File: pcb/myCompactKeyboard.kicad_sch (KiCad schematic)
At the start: 292 parts, among them J1 OLED_128x64, SW1 RotaryEncoder_Switch, SW2 RotaryEncoder_Switch, U1 Raspberry_Pi_Pico

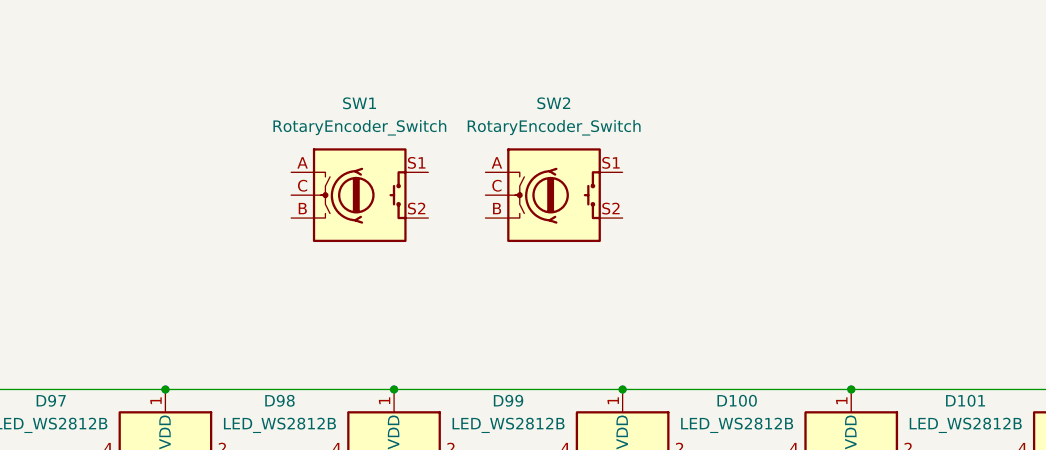
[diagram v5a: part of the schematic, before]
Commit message: added labels to rotary encoders
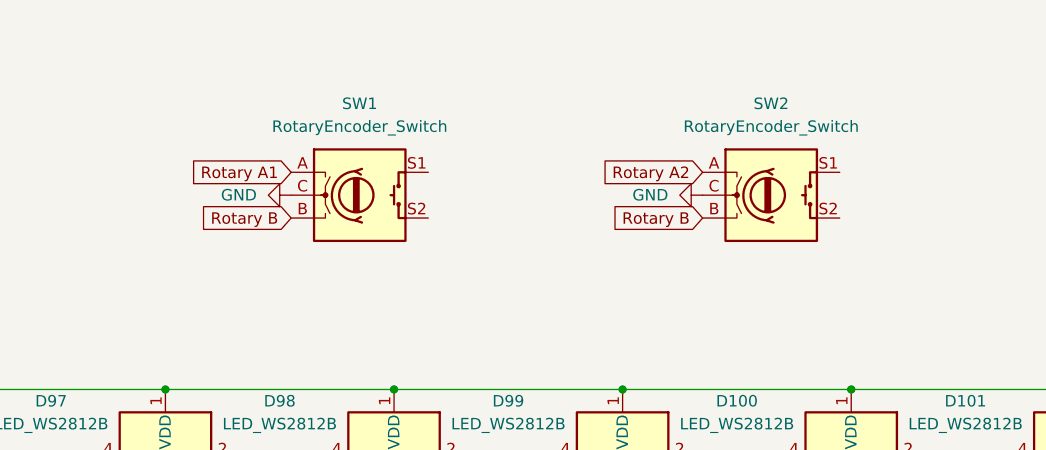
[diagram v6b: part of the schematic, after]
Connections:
- net GND: now also SW1.C, SW2.C
- net Rotary A2: now reaches SW2.A
- net Rotary B: now reaches SW2.B
- net Rotary B: now also SW1.B
- net Rotary A1: now reaches SW1.A
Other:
- moved on the sheet: SW2
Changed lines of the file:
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@@
 		)
 	)
+	(global_label "Rotary B"
+		(shape input)
+		(at 326.39 49.53 180)
+		(fields_autoplaced yes)
+		(effects
+			(font
+				(size 1.27 1.27)
+			)
+			(justify right)
+		)
+		(property "Intersheetrefs" "${INTERSHEET_REFS}"
+			(at 315.1197 49.53 0)
+			(effects
+				(font
+					(size 1.27 1.27)
+				)
+				(justify right)
+				(hide yes)
+			)
+		)
+	)
 	(global_label "Col 4"
 		(shape input)
@@
 		)
 	)
+	(global_label "Rotary A1"
+		(shape input)
+		(at 280.67 44.45 180)
+		(fields_autoplaced yes)
+		(effects
+			(font
+				(size 1.27 1.27)
+			)
+			(justify right)
+		)
+		(property "Intersheetrefs" "${INTERSHEET_REFS}"
+			(at 268.3716 44.45 0)
+			(effects
+				(font
+					(size 1.27 1.27)
+				)
+				(justify right)
+				(hide yes)
+			)
+		)
+	)
 	(global_label "Col 12"
 		(shape input)
@@
 		)
 	)
+	(global_label "Rotary B"
+		(shape input)
+		(at 280.67 49.53 180)
+		(fields_autoplaced yes)
+		(effects
+			(font
+				(size 1.27 1.27)
+			)
+			(justify right)
+		)
+		(property "Intersheetrefs" "${INTERSHEET_REFS}"
+			(at 269.3997 49.53 0)
+			(effects
+				(font
+					(size 1.27 1.27)
+				)
+				(justify right)
+				(hide yes)
+			)
+		)
+	)
 	(global_label "Col 11"
 		(shape input)
@@
 		)
 	)
+	(global_label "Rotary A2"
+		(shape input)
+		(at 326.39 44.45 180)
+		(fields_autoplaced yes)
+		(effects
+			(font
+				(size 1.27 1.27)
+			)
+			(justify right)
+		)
+		(property "Intersheetrefs" "${INTERSHEET_REFS}"
+			(at 314.0916 44.45 0)
+			(effects
+				(font
+					(size 1.27 1.27)
+				)
+				(justify right)
+				(hide yes)
+			)
+		)
+	)
 	(global_label "Row 8"
 		(shape input)
@@
 	(symbol
 		(lib_id "Device:RotaryEncoder_Switch")
-		(at 309.88 46.99 0)
+		(at 334.01 46.99 0)
 		(unit 1)
 		(exclude_from_sim no)
@@
 		(fields_autoplaced yes)
 		(property "Reference" "SW2"
-			(at 309.88 36.83 0)
+			(at 334.01 36.83 0)
 			(effects
 				(font
@@
 		)
 		(property "Value" "RotaryEncoder_Switch"
-			(at 309.88 39.37 0)
+			(at 334.01 39.37 0)
 			(effects
 				(font
@@
 		)
 		(property "Footprint" ""
-			(at 306.07 42.926 0)
+			(at 330.2 42.926 0)
 			(effects
 				(font
@@
 		)
 		(property "Datasheet" "~"
-			(at 309.88 40.386 0)
+			(at 334.01 40.386 0)
 			(effects
 				(font
@@
 		)
 		(property "Description" "Rotary encoder, dual channel, incremental quadrate outputs, with switch"
-			(at 309.88 46.99 0)
+			(at 334.01 46.99 0)
 			(effects
 				(font
@@
 	)
 	(symbol
+		(lib_id "power:GND")
+		(at 280.67 46.99 270)
+		(unit 1)
+		(exclude_from_sim no)
+		(in_bom yes)
+		(on_board yes)
+		(dnp no)
+		(fields_autoplaced yes)
+		(property "Reference" "#PWR06"
+			(at 274.32 46.99 0)
+			(effects
+				(font
+					(size 1.27 1.27)
+				)
+				(hide yes)
+			)
+		)
+		(property "Value" "GND"
+			(at 276.86 46.9899 90)
+			(effects
+				(font
+					(size 1.27 1.27)
+				)
+				(justify right)
+			)
+		)
+		(property "Footprint" ""
+			(at 280.67 46.99 0)
+			(effects
+				(font
+					(size 1.27 1.27)
+				)
+				(hide yes)
+			)
+		)
+		(property "Datasheet" ""
+			(at 280.67 46.99 0)
+			(effects
+				(font
+					(size 1.27 1.27)
+				)
+				(hide yes)
+			)
+		)
+		(property "Description" "Power symbol creates a global label with name \"GND\" , ground"
+			(at 280.67 46.99 0)
+			(effects
+				(font
+					(size 1.27 1.27)
+				)
+				(hide yes)
+			)
+		)
+		(pin "1"
+		)
+		(instances
+			(project ""
+				(path "/a5f71a14-17d5-4701-ba70-d64b25a756b2"
+					(reference "#PWR06")
+					(unit 1)
+				)
+			)
+		)
+	)
+	(symbol
 		(lib_id "ScottoKeebs:Placeholder_Diode")
 		(at 68.58 59.69 90)
@@
 					(unit 1)
 				)
+			)
+		)
+	)
+	(symbol
+		(lib_id "power:GND")
+		(at 326.39 46.99 270)
+		(unit 1)
+		(exclude_from_sim no)
+		(in_bom yes)
+		(on_board yes)
+		(dnp no)
+		(fields_autoplaced yes)
+		(property "Reference" "#PWR07"
+			(at 320.04 46.99 0)
+			(effects
+				(font
+					(size 1.27 1.27)
+				)
+				(hide yes)
+			)
+		)
+		(property "Value" "GND"
+			(at 322.58 46.9899 90)
+			(effects
+				(font
+					(size 1.27 1.27)
+				)
+				(justify right)
+			)
+		)
+		(property "Footprint" ""
+			(at 326.39 46.99 0)
+			(effects
+				(font
+					(size 1.27 1.27)
+				)
+				(hide yes)
+			)
+		)
+		(property "Datasheet" ""
+			(at 326.39 46.99 0)
+			(effects
+				(font
+					(size 1.27 1.27)
+				)
+				(hide yes)
+			)
+		)
+		(property "Description" "Power symbol creates a global label with name \"GND\" , ground"
+			(at 326.39 46.99 0)
+			(effects
+				(font
+					(size 1.27 1.27)
+				)
+				(hide yes)
+			)
+		)
+		(pin "1"
+		)
+		(instances
+			(project ""
+				(path "/a5f71a14-17d5-4701-ba70-d64b25a756b2"
+					(reference "#PWR07")
+					(unit 1)
+				)

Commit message: created pcb and placed switches
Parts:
- removed S82, S86: Keyswitch, ScottoKeebs_MX:MX_PCB_1.00u, symbol ScottoKeebs:Placeholder_Keyswitch
- SW1, SW2: footprint (none) -> Rotary_Encoder:RotaryEncoder_Alps_EC11E-Switch_Vertical_H20mm
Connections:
- net +5V: now also J1.2 (VCC)
- net Col 10: now also SW2.S1
- net Col 9: now also SW1.S1
- net GND: now also J1.1 (GND)
- net WS_Led: now also U1.29 (GPIO22); no longer U1.26 (GPIO20)
- net at SW2.S2: now also D86.2 (A)
- net at SW1.S2: now also D82.2 (A)
- net SCL: now reaches U1.27 (GPIO21)
- net SCL: now also J1.3 (SCL)
- net SDA: now reaches J1.4 (SDA)
- net SDA: now also U1.26 (GPIO20)
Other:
- moved on the sheet: D10, D100, D101, D102, D103, D104, D105, D106, D107, D108, D109, D11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

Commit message: placed all elements on pcb and started wiring
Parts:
- D100, D101, D102, D103, D104, D105, D106, D107, D108, D109, D110, D111, D112, D113, D114, D115, D116, D117, D118, D119, D120, D121, D122, D123, D124, D125, D126, D127, D128, D129, D130, D131, D132, D133, D134, D135, D136, D137, D138, D139, D140, D141, D142, D143, D144, D145, D146, D147, D148, D149, D150, D151, D152, D153, D154, D155, D156, D157, D158, D159, D160, D161, D162, D163, D164, D165, D166, D167, D168, D169, D170, D171, D172, D173, D174, D175, D176, D177, D178, D179, D180, D181, D182, D183, D184, D185, D186, D187, D188, D189, D190, D191, D192, D97, D98, D99: footprint ScottoKeebs_Components:LED_WS2812B -> leds:SK6812MINI-E
